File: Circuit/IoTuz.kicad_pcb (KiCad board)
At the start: 2 copper layers, 150 x 95 mm, 100 parts, among them J1 Jack.3.5mm-Mono, P1 ALLIGATOR_X39, P2 BATTERY, P3 USB_5PIN_SHELL, P4 LED_1, P5 LED_2, P8 IRReceiver, Q1 S8050, Q2 S8050, Q202 FDN340P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

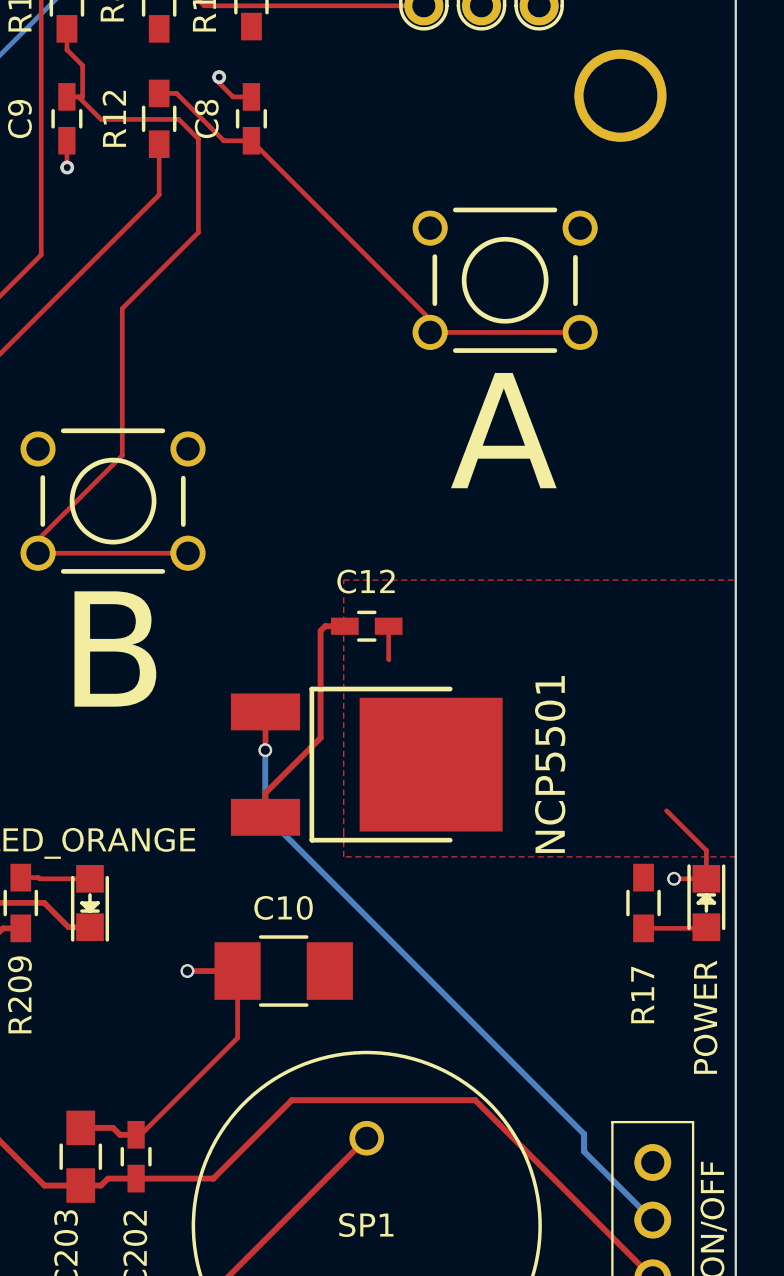
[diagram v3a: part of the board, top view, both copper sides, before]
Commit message: Changing pour and placement around LDO.
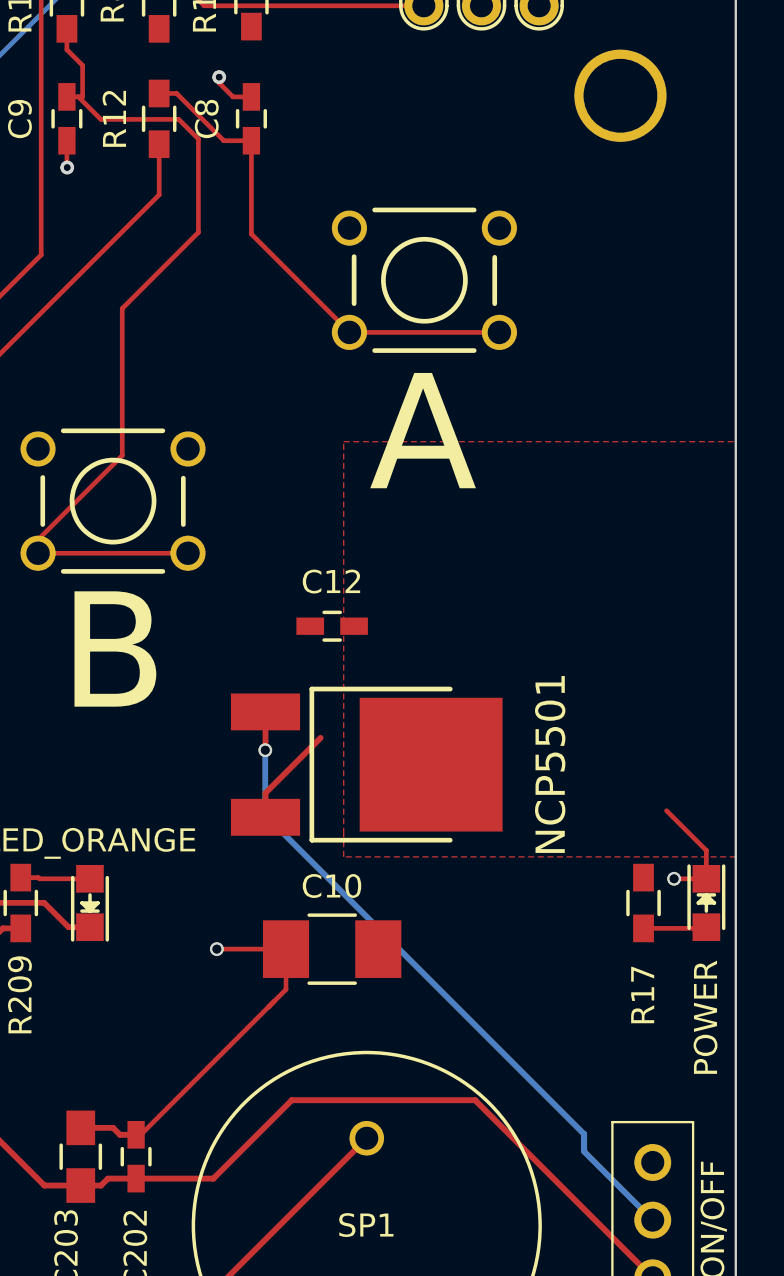
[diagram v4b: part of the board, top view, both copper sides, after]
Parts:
- moved SW4 3.50 mm to (186.5, 86.0)
- moved C10 2.30 mm to (182.5, 115.0)
- moved C12 1.50 mm to (182.5, 101.0)
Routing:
- net +3V3: track 142.4 -> 136.6 mm
- net GND: track 217.9 -> 220.0 mm
- net Net-(C8-Pad1): track 22.9 -> 21.4 mm
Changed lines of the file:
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@@
   (general
     (links 389)
-    (no_connects 47)
+    (no_connects 49)
     (area 0 34.300001 200.408 183.955)
     (thickness 1.6)
     (drawings 219)
-    (tracks 1376)
+    (tracks 1375)
     (zones 0)
     (modules 100)
@@
   )
   (setup
-    (last_trace_width 0.254)
+    (last_trace_width 0.2032)
     (user_trace_width 0.2032)
     (user_trace_width 0.254)
@@
   )
   (module freetronics_footprints:SW_PUSHBUTTON_PTH (layer F.Cu)
-    (at 190 86)
+    (at 186.5 86)
     (descr "<b>OMRON SWITCH</b>")
     (fp_text reference SW4 (at -0.05 0) (layer Eco1.User)
@@
   )
   (module Capacitors_SMD:C_1210_HandSoldering (layer F.Cu)
-    (at 180.4 115.95)
+    (at 182.5 115)
     (descr "Capacitor SMD 1210, hand soldering")
     (tags "capacitor 1210")
@@
   )
   (module Capacitors_SMD:C_0603_HandSoldering (layer F.Cu)
-    (at 184 101)
+    (at 182.5 101)
     (descr "Capacitor SMD 0603, hand soldering")
     (tags "capacitor 0603")
@@
   (via (at 162.5 64.7) (size 0.6) (layers F.Cu B.Cu) (net 1))
   (segment (start 162.035 64.235) (end 162.5 64.7) (width 0.2032) (layer F.Cu) (net 1))
-  (segment (start 182 101.196) (end 182 105.841) (width 0.254) (layer F.Cu) (net 1))
   (segment (start 182 105.841) (end 179.61 108.231) (width 0.254) (layer F.Cu) (net 1))
   (segment (start 179.61 108.231) (end 179.61 109.285) (width 0.254) (layer F.Cu) (net 1) (status 20))
-  (segment (start 183.05 101) (end 182.196 101) (width 0.254) (layer F.Cu) (net 1) (status 10))
-  (segment (start 182.196 101) (end 182 101.196) (width 0.254) (layer F.Cu) (net 1))
   (via (at 78.75 116.5) (size 0.6) (drill 0.4) (layers F.Cu B.Cu) (net 1))
   (segment (start 78.75 119) (end 78.75 116.5) (width 0.254) (layer B.Cu) (net 1))
@@
   (segment (start 86 62.9) (end 85.9004 62.9) (width 0.2032) (layer F.Cu) (net 1) (status 30))
   (segment (start 100 95.9) (end 100 96.05) (width 0.2032) (layer F.Cu) (net 1) (status 30))
+  (segment (start 174.2 123.05) (end 179.75 117.5) (width 0.2032) (layer F.Cu) (net 2))
+  (segment (start 179.75 117.5) (end 180 117.25) (width 0.2032) (layer F.Cu) (net 2))
+  (segment (start 180.5 115) (end 180.5 116.75) (width 0.2032) (layer F.Cu) (net 2))
+  (segment (start 180.5 116.75) (end 179.75 117.5) (width 0.2032) (layer F.Cu) (net 2))
+  (segment (start 180.5 115) (end 177.500008 115) (width 0.2032) (layer F.Cu) (net 2))
+  (segment (start 177.500008 115) (end 177.5 115.000008) (width 0.2032) (layer F.Cu) (net 2))
+  (segment (start 180 115.95) (end 180 115.300007) (width 0.254) (layer F.Cu) (net 2))
+  (via (at 177.5 115.000008) (size 0.6) (drill 0.4) (layers F.Cu B.Cu) (net 2))
+  (segment (start 174 123.05) (end 174.2 123.05) (width 0.2032) (layer F.Cu) (net 2))
   (via (at 142.14599 102.825) (size 0.6) (drill 0.4) (layers F.Cu B.Cu) (net 2))
   (segment (start 141.1 102.825) (end 142.14599 102.825) (width 0.2032) (layer F.Cu) (net 2))
-  (segment (start 142.59842 111.095) (end 140.305 111.095) (width 0.254) (layer F.Cu) (net 2) (status 400000))
+  (segment (start 142.59842 111.095) (end 140.305 111.095) (width 0.254) (layer F.Cu) (net 2))
   (via (at 140.3 111.1) (size 0.6) (drill 0.4) (layers F.Cu B.Cu) (net 2))
   (segment (start 140.305 111.095) (end 140.3 111.1) (width 0.254) (layer F.Cu) (net 2))
   (segment (start 174.35 134.45) (end 175.55 134.45) (width 0.254) (layer F.Cu) (net 2))
   (via (at 175.55 134.45) (size 0.6) (drill 0.4) (layers F.Cu B.Cu) (net 2))
-  (segment (start 178.4 115.95) (end 176.225 115.95) (width 0.254) (layer F.Cu) (net 2))
-  (via (at 176.225 115.95) (size 0.6) (drill 0.4) (layers F.Cu B.Cu) (net 2))
   (via (at 125.7 104.875) (size 0.6) (drill 0.4) (layers F.Cu B.Cu) (net 2))
   (segment (start 126.2 104.375) (end 125.7 104.875) (width 0.254) (layer F.Cu) (net 2))
@@
   (via (at 197.325 111.95) (size 0.6) (drill 0.4) (layers F.Cu B.Cu) (net 2))
   (segment (start 197.32598 111.95098) (end 197.325 111.95) (width 0.2032) (layer F.Cu) (net 2))
-  (segment (start 174 123.05) (end 174.2 123.05) (width 0.2032) (layer F.Cu) (net 2))
-  (segment (start 174.2 123.05) (end 178.4 118.85) (width 0.2032) (layer F.Cu) (net 2))
-  (segment (start 178.4 118.85) (end 178.4 115.95) (width 0.2032) (layer F.Cu) (net 2))
   (segment (start 126.75 114.621) (end 126.75 116.6198) (width 0.254) (layer F.Cu) (net 2))
   (via (at 126.75 116.6198) (size 0.6) (drill 0.4) (layers F.Cu B.Cu) (net 2))
@@
   (segment (start 198.725 111.95098) (end 198.725 110.725) (width 0.2032) (layer F.Cu) (net 2) (status 10))
   (segment (start 198.725 110.725) (end 197 109) (width 0.2032) (layer F.Cu) (net 2) (status 20))
-  (segment (start 184.95 102.435225) (end 184.963845 102.44907) (width 0.2032) (layer F.Cu) (net 2))
-  (segment (start 184.95 101) (end 184.95 102.435225) (width 0.2032) (layer F.Cu) (net 2) (status 10))
   (segment (start 66.727776 126.95) (end 67.744961 127.967185) (width 0.2032) (layer F.Cu) (net 2))
   (segment (start 66.25 126.95) (end 66.727776 126.95) (width 0.2032) (layer F.Cu) (net 2) (status 10))
@@
   (segment (start 63.8521 97.597) (end 57.8748 97.597) (width 0.2032) (layer F.Cu) (net 4))
   (segment (start 63.9 97.6449) (end 63.8521 97.597) (width 0.2032) (layer F.Cu) (net 4))
-  (segment (start 193.2512 88.2606) (end 186.7488 88.2606) (width 0.2032) (layer F.Cu) (net 5))
-  (segment (start 186.7488 88.2606) (end 186.7488 87.6988) (width 0.2032) (layer F.Cu) (net 5))
-  (segment (start 186.7488 87.6988) (end 179 79.95) (width 0.2032) (layer F.Cu) (net 5))
+  (segment (start 189.7512 88.2606) (end 183.2488 88.2606) (width 0.2032) (layer F.Cu) (net 5))
+  (segment (start 183.2606 88.2606) (end 179 84) (width 0.2032) (layer F.Cu) (net 5))
+  (segment (start 179 84) (end 179 79.95) (width 0.2032) (layer F.Cu) (net 5))
   (segment (start 177.805 79.95) (end 179 79.95) (width 0.2032) (layer F.Cu) (net 5) (status 20))
   (segment (start 175.755 77.9) (end 177.805 79.95) (width 0.2032) (layer F.Cu) (net 5))
@@
     (polygon
       (pts
-        (xy 183 110) (xy 183 99) (xy 200 99) (xy 200 111) (xy 183 111)
+        (xy 183 110) (xy 183 93) (xy 200 93) (xy 200 111) (xy 183 111)
       )
     )

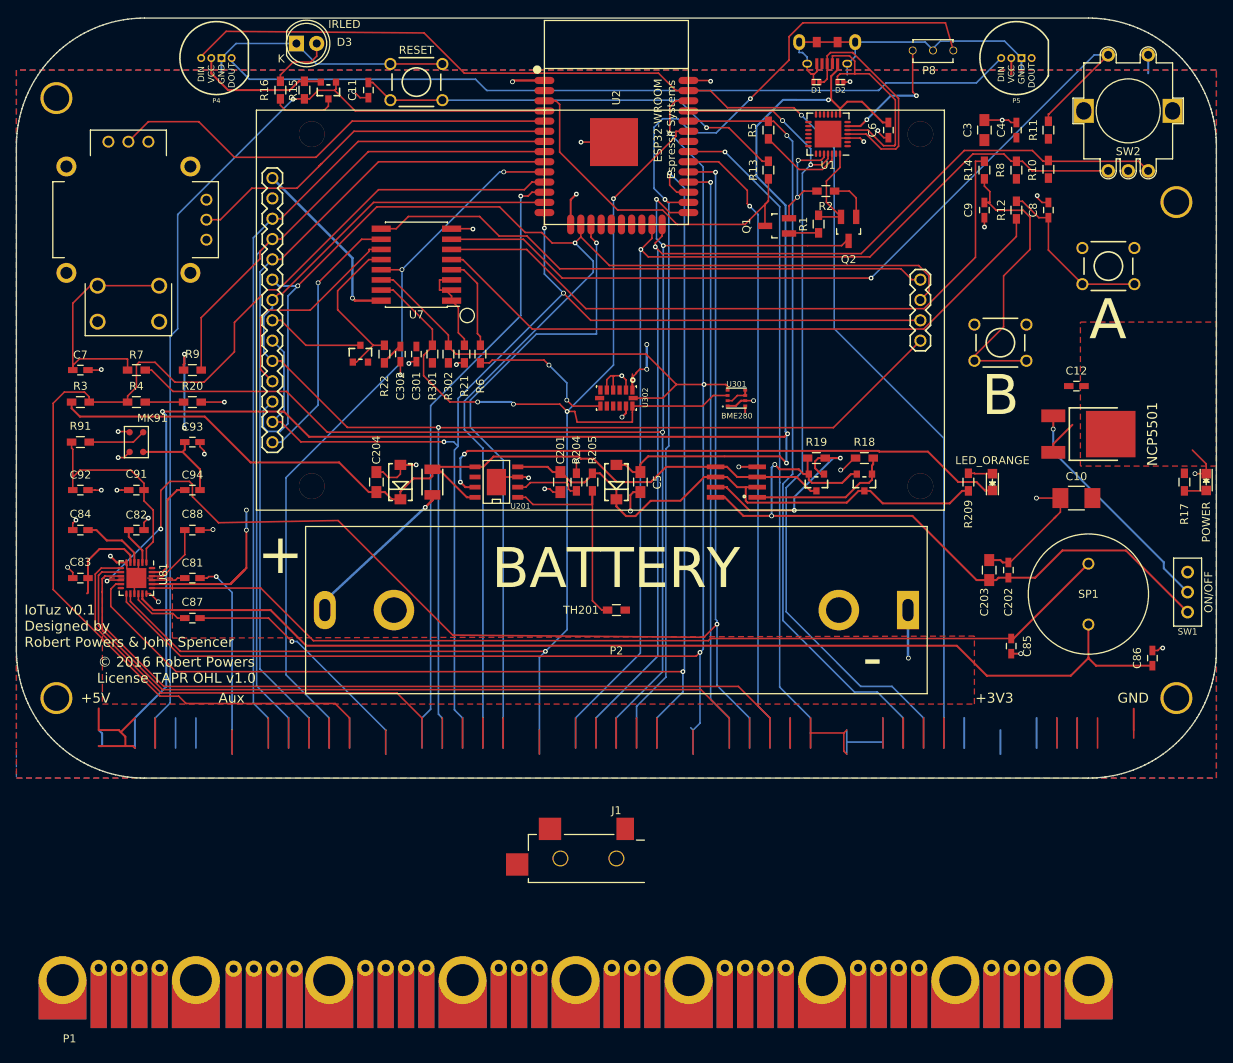
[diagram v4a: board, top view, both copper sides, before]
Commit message: Changes to v0.1 pinout errors. v0.1->Minimal vNext changes. Most routing reworked. Closes #12, closes #18, closes #19, closes #21.
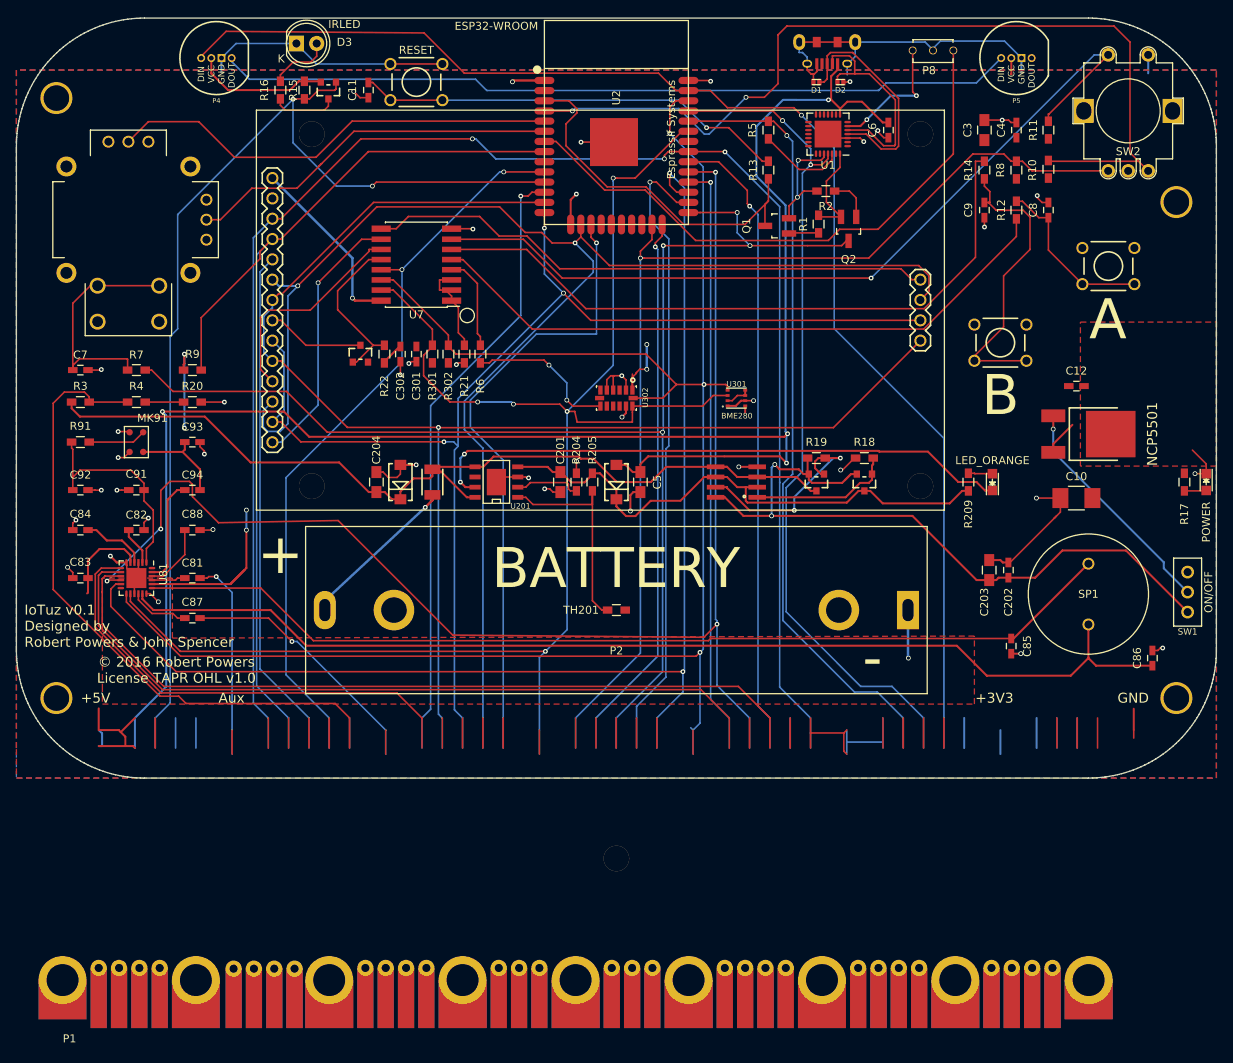
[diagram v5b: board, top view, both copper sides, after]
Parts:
- removed J1: Jack.3.5mm-Mono, libs:3.5mmMonoTSJack.MJ-3523-SMT.Switch
- added MP4: M3, libs:MountingHole_3.2mm_M3.IoTuz, F.Cu at (125.0, 160.1)
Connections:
- P8 pad 1: /IO4 -> /IO35
- Q4 pad G: /Sensor_VP -> /IO26
- R10 pad 1: /IO2 -> /Sensor_VP
- R15 pad 2: /Sensor_VP -> /IO26
- R3 pad 2: /IO26 -> /IO2
- R4 pad 2: /IO26 -> /IO2
- SW2 pad 3: /IO2 -> /Sensor_VP
- U6 pad 3: /IO35 -> /IO19
- U6 pad 5: /IO33 -> /IO4
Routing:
- net /IO19: track 83.5 -> 209.2 mm, vias 1 -> 3
- net /IO33: track 103.3 -> 0.00 mm
- net /IO35: track 105.9 -> 73.7 mm
- net /IO26: track 151.3 -> 134.3 mm, vias 0 -> 2
- net /IO2: track 137.5 -> 150.6 mm
- net /IO4: track 131.7 -> 143.5 mm, vias 2 -> 1
- net /Sensor_VP: track 122.3 -> 113.0 mm, vias 1 -> 2
- net /I2C_SDA: track 200.1 -> 201.2 mm
- net /EN: track 45.2 -> 46.3 mm
- net /IO0: vias 3 -> 4

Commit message: Added 10k resistors on pins from quadrature out on encoder. Fixes #16.
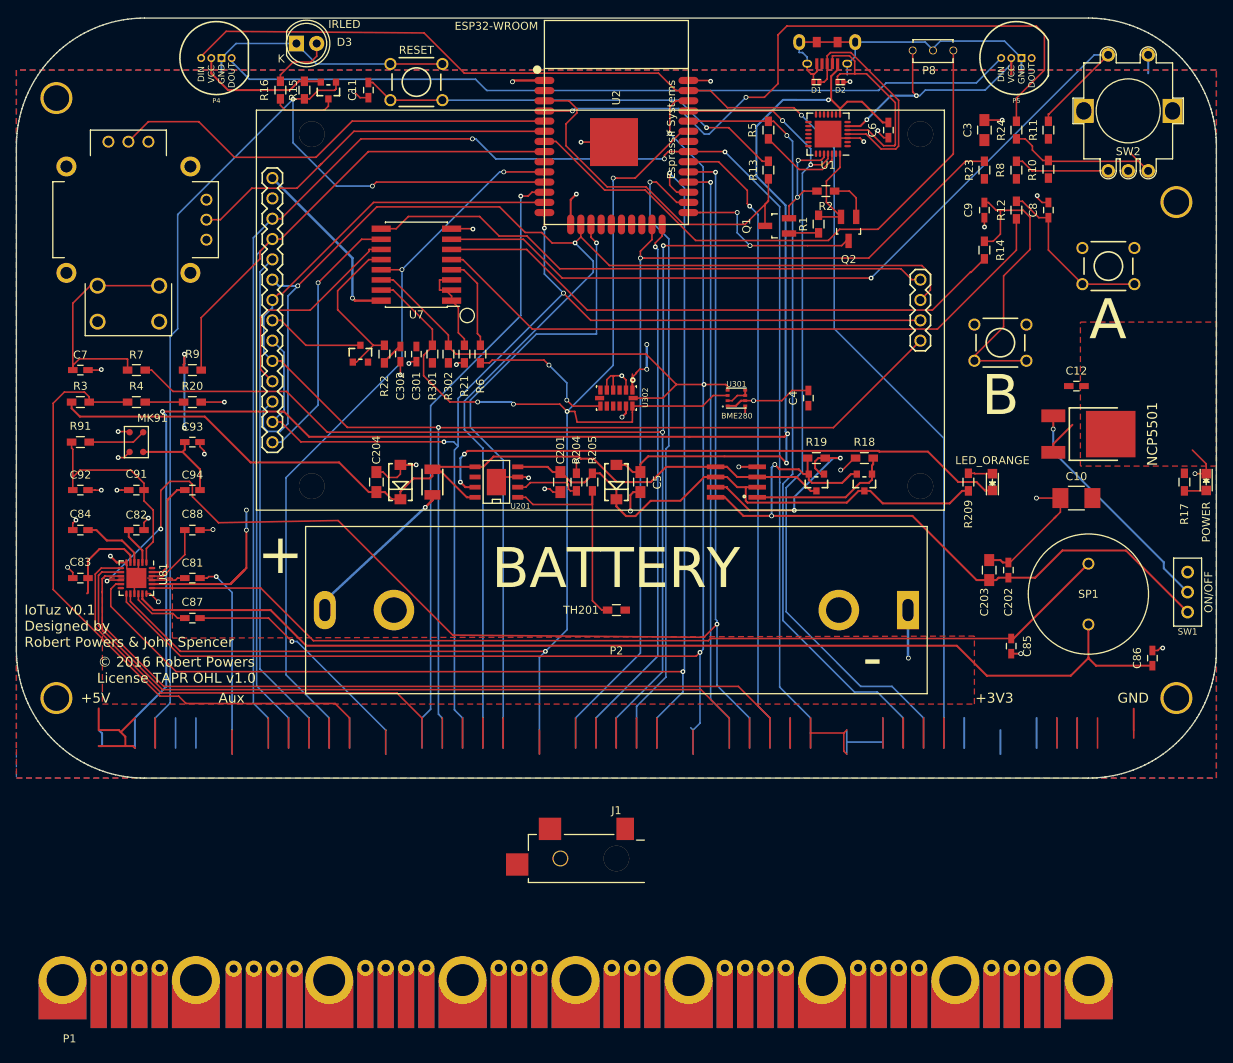
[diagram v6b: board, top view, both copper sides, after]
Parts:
- added J1: Jack.3.5mm-Mono, libs:3.5mmMonoTSJack.MJ-3523-SMT.Switch, F.Cu at (125.0, 160.1)
- added R23: 10K, Resistors_SMD:R_0603_HandSoldering, F.Cu at (171.0, 74.0)
- added R24: 10K, Resistors_SMD:R_0603_HandSoldering, F.Cu at (175.0, 69.0)
- moved C4 42.4 mm to (149.0, 102.5)
- moved R14 10.0 mm to (171.0, 84.0), turned to 90 degrees
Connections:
- R10 pad 1: /Sensor_VP -> Net-(R10-Pad1)
- R8 pad 1: /IO15 -> Net-(R23-Pad1)
- SW2 pad 1: /IO15 -> Net-(R23-Pad1)
- SW2 pad 3: /Sensor_VP -> Net-(R10-Pad1)
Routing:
- net /Sensor_VP: track 113.0 -> 85.9 mm
- net Net-(R10-Pad1): track 0.00 -> 19.9 mm
- net /IO15: track 134.1 -> 117.4 mm
- net +3V3: track 136.6 -> 150.9 mm
- net Net-(R23-Pad1): track 0.00 -> 12.0 mm
- net /B_Btn: track 84.3 -> 72.4 mm
- net GND: track 220.0 -> 225.5 mm
- net Net-(C9-Pad1): track 37.2 -> 39.1 mm
- net /A_Btn: track 81.2 -> 82.2 mm
